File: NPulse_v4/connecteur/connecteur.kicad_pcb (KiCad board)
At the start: 4 copper layers, 39.8 x 44 mm, 74 parts, among them J1 Conn_01x01, J10 Conn_02x05_Odd_Even, J11 Conn_01x01, J12 Conn_01x01, J13 Conn_02x05_Odd_Even, J14 Conn_01x01, J15 Conn_01x01, J16 Conn_01x01, J17 Conn_01x01, J18 Conn_01x01, J19 Conn_01x01, J2 Conn_01x01, J20 Conn_01x01, J21 Conn_01x01, J22 Conn_01x01, J23 Conn_01x01, J25 Conn_01x01, J26 Conn_01x01, J27 Conn_01x01, J29 Conn_01x01, J3 Conn_01x01, J30 Conn_01x01, J32 Conn_02x05_Odd_Even, J34 Conn_01x01, J35 Conn_02x05_Odd_Even, J36 Conn_01x01, J37 Conn_01x01, J38 Conn_01x01, J39 Conn_01x01, J4 Conn_01x01, J40 Conn_01x01, J41 Conn_01x01, J42 Conn_01x01, J43 Conn_01x01, J44 Conn_01x01, J45 Conn_01x01, J46 Conn_01x01, J47 Conn_01x01, J48 Conn_01x01, J49 Conn_01x01, J5 Conn_01x01, J50 Conn_01x01, J51 Conn_01x01, J52 Conn_01x01, J53 Conn_01x01, J54 Conn_02x05_Odd_Even, J55 Conn_01x01, J56 Conn_01x01, J57 Conn_02x05_Odd_Even, J58 Conn_01x01, J59 Conn_01x01, J6 Conn_01x01, J60 Conn_01x01, J61 Conn_01x01, J62 Conn_01x01, J63 Conn_01x01, J64 Conn_01x01, J65 Conn_01x01, J66 Conn_01x01, J67 Conn_01x01, J68 Conn_01x01, J69 Conn_01x01, J7 Conn_01x01, J70 Conn_01x01, J72 Conn_01x01, J73 Conn_01x01, J74 Conn_01x01, J75 Conn_01x01, J76 Conn_01x01, J8 Conn_01x01, J9 Conn_01x01

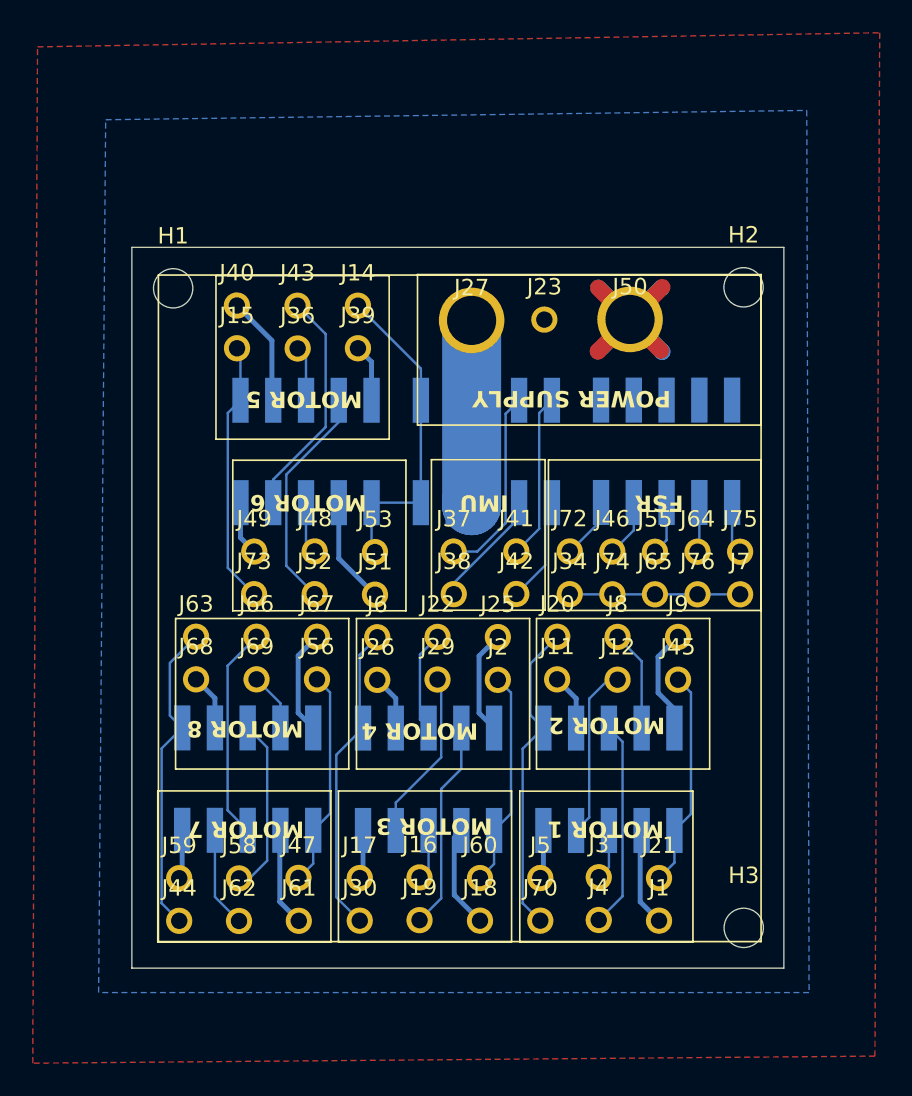
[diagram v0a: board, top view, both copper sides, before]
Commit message: Correct LDO schematic and update connectors to through-hole footprints
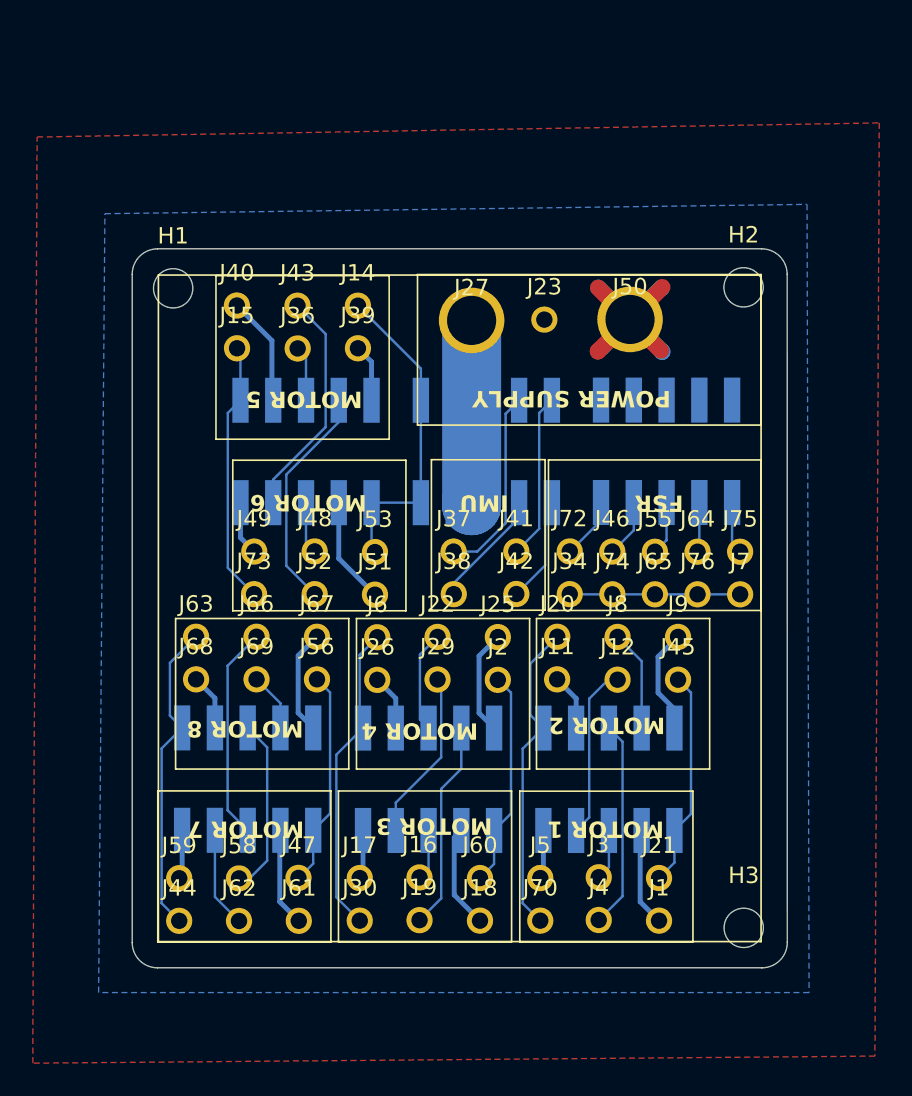
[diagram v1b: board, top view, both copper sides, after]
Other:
- board size 39.8 x 44 mm -> 40 x 43.9 mm
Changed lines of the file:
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@@
 		(stroke
 			(width 0.1)
-			(type default)
+			(type solid)
 		)
 		(fill no)
@@
 		(layer "F.SilkS")
 	)
-	(gr_rect
-		(start 147.3 79.84)
-		(end 187.1 123.84)
+	(gr_arc
+		(start 147.32 81.48)
+		(mid 147.773984 80.383984)
+		(end 148.87 79.93)
 		(stroke
 			(width 0.05)
 			(type default)
 		)
-		(fill no)
-		(locked yes)
+		(layer "Edge.Cuts")
+	)
+	(gr_line
+		(start 187.3 81.48)
+		(end 187.31 122.27)
+		(stroke
+			(width 0.05)
+			(type default)
+		)
+		(layer "Edge.Cuts")
+	)
+	(gr_arc
+		(start 185.75 79.93)
+		(mid 186.846016 80.383984)
+		(end 187.3 81.48)
+		(stroke
+			(width 0.05)
+			(type default)
+		)
+		(layer "Edge.Cuts")
+	)
+	(gr_line
+		(start 147.32 122.28)
+		(end 147.32 81.48)
+		(stroke
+			(width 0.05)
+			(type default)
+		)
+		(layer "Edge.Cuts")
+	)
+	(gr_line
+		(start 185.76 123.82)
+		(end 148.86 123.82)
+		(stroke
+			(width 0.05)
+			(type default)
+		)
+		(layer "Edge.Cuts")
+	)
+	(gr_line
+		(start 148.87 79.93)
+		(end 185.75 79.93)
+		(stroke
+			(width 0.05)
+			(type default)
+		)
+		(layer "Edge.Cuts")
+	)
+	(gr_arc
+		(start 187.31 122.27)
+		(mid 186.856016 123.366016)
+		(end 185.76 123.82)
+		(stroke
+			(width 0.05)
+			(type default)
+		)
+		(layer "Edge.Cuts")
+	)
+	(gr_arc
+		(start 148.86 123.82)
+		(mid 147.771056 123.368944)
+		(end 147.32 122.28)
+		(stroke
+			(width 0.05)
+			(type default)
+		)
 		(layer "Edge.Cuts")
 	)
@@
 		(polygon
 			(pts
-				(xy 141.54 67.6) (xy 192.95 66.74) (xy 192.66 129.21) (xy 141.25 129.64)
+				(xy 141.514274 73.103498) (xy 192.924452 72.243495) (xy 192.66 129.21) (xy 141.25 129.64)
 			)
 		)
@@
 		(polygon
 			(pts
-				(xy 145.7 72.05) (xy 188.5 71.48) (xy 188.64 125.33) (xy 145.27 125.33)
+				(xy 145.65371 77.785689) (xy 188.51491 77.214873) (xy 188.64 125.33) (xy 145.27 125.33)
 			)
 		)
@@
 		(polygon
 			(pts
-				(xy 142.83 69.18) (xy 191.51 68.32) (xy 191.51 128.2) (xy 142.83 128.2)
+				(xy 142.83 74.688658) (xy 191.51 73.828658) (xy 191.51 128.2) (xy 142.83 128.2)
 			)
 		)
@@
 		(polygon
 			(pts
-				(xy 144.41 70.47) (xy 190.08 69.9) (xy 190.08 127.05) (xy 144.12 126.77)
+				(xy 144.379327 76.424764) (xy 190.08 75.854382) (xy 190.08 127.05) (xy 144.12 126.77)
 			)
 		)
